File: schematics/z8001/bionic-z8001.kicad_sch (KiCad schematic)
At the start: 9 parts, among them J1 BionicConnector, U1 Z8001, U2 74HCT126, U3 74HCT541, U4 74HCT541

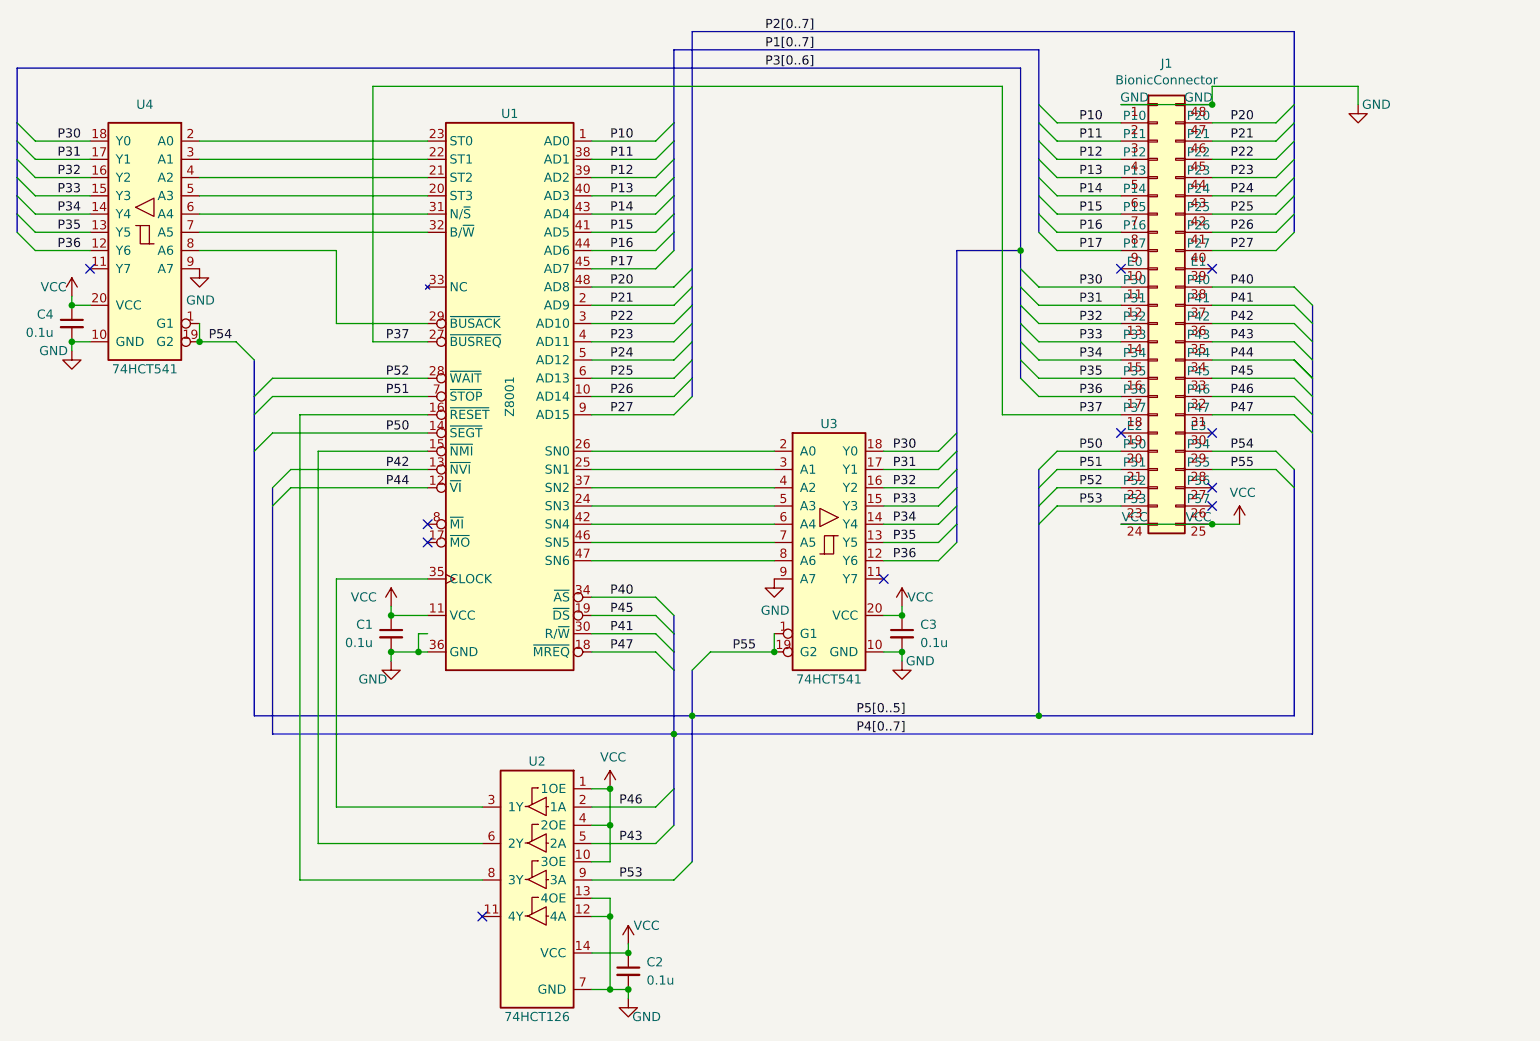
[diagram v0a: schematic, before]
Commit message: [Z8001] Move schematics directory
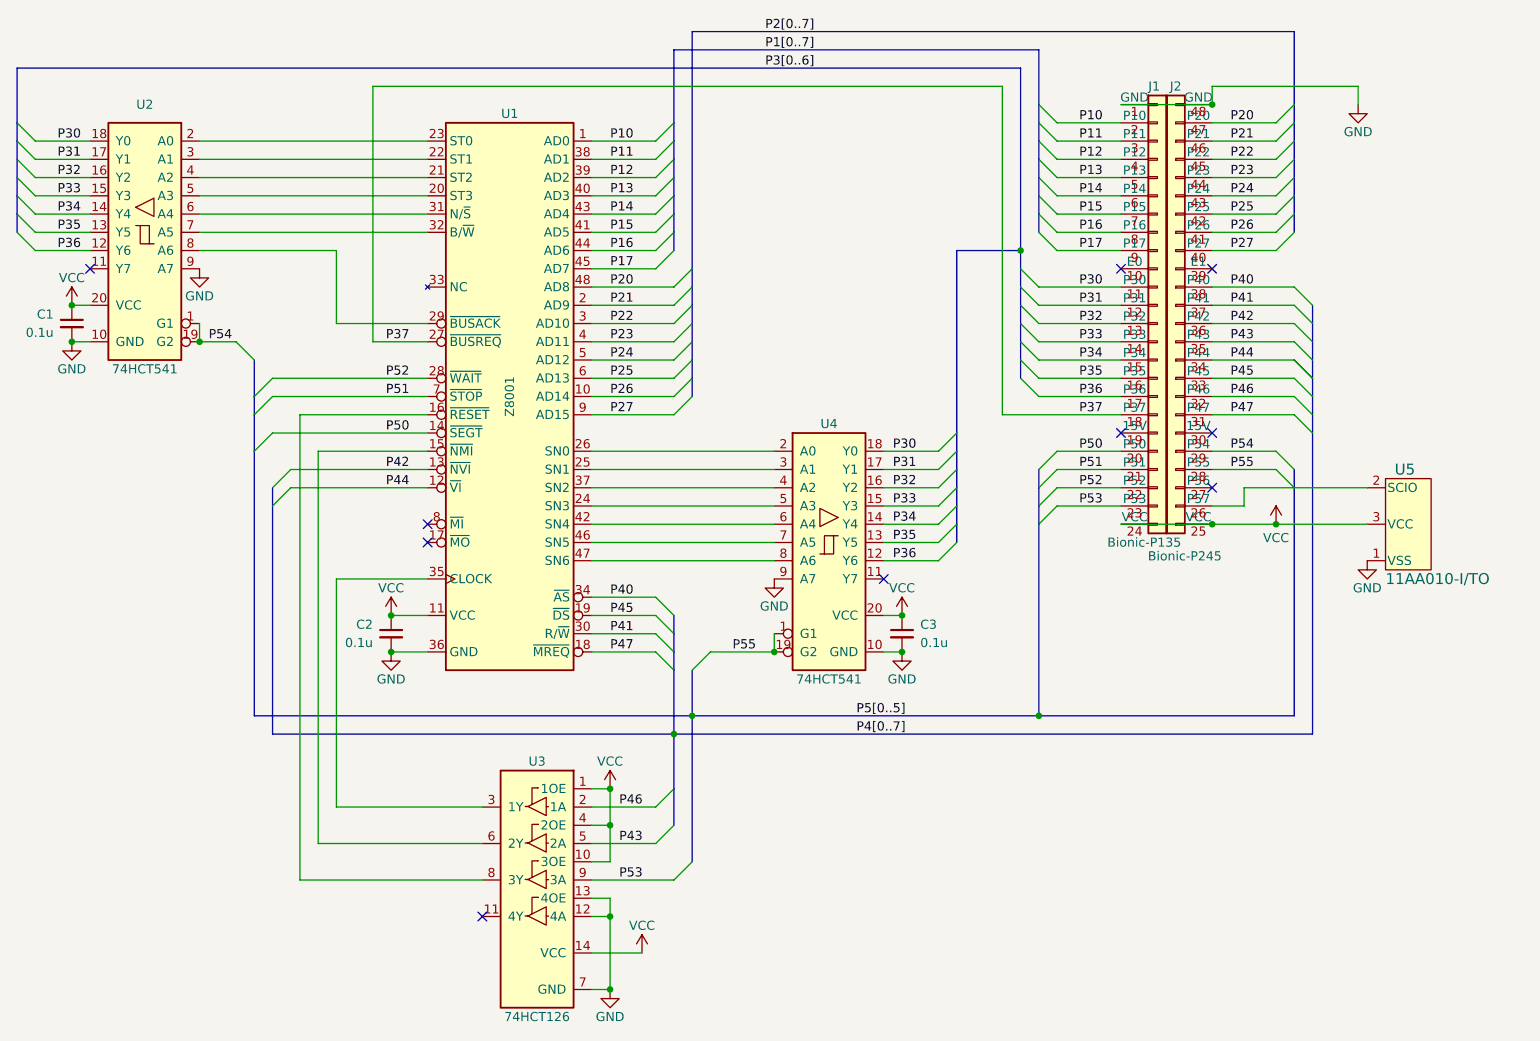
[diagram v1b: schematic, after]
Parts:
- removed C2: 0.1u, Capacitor_THT:C_Disc_D3.4mm_W2.1mm_P2.50mm, symbol Device:C_Small
- removed J1: BionicConnector, 0-LocalLibrary:DIP-48_W7.62mm, symbol 0-LocalLibrary:BionicConnector
- added J1: Bionic-P135, connector:Bionic-P135_Vertical, symbol 0-LocalLibrary:Bionic-P135
- added J2: Bionic-P245, connector:Bionic-P245_Vertical, symbol 0-LocalLibrary:Bionic-P245
- added U5: 11AA010-I/TO, TO-92_MC_MCH, symbol 0-LocalLibrary:11AA010-I_TO
- renumbered C4 to C1, C1 to C2, U4 to U2, U2 to U3, U3 to U4
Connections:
- net GND: now also J1.1 (GND), J2.48 (GND), U5.1 (VSS)
- net P10: now also J1.2 (P10)
- net P11: now also J1.3 (P11)
- net P12: now also J1.4 (P12)
- net P13: now also J1.5 (P13)
- net P14: now also J1.6 (P14)
- net P15: now also J1.7 (P15)
- net P16: now also J1.8 (P16)
- net P17: now also J1.9 (P17)
- net P20: now also J2.47 (P20)
- net P21: now also J2.46 (P21)
- net P22: now also J2.45 (P22)
- net P23: now also J2.44 (P23)
- net P24: now also J2.43 (P24)
- net P25: now also J2.42 (P25)
- net P26: now also J2.41 (P26)
- net P27: now also J2.40 (P27)
- net P30: now also J1.11 (P30)
- net P31: now also J1.12 (P31)
- net P32: now also J1.13 (P32)
- net P33: now also J1.14 (P33)
- net P34: now also J1.15 (P34)
- net P35: now also J1.16 (P35)
- net P36: now also J1.17 (P36)
- net P37: now also J1.18 (P37)
- net P40: now also J2.38 (P40)
- net P41: now also J2.37 (P41)
- net P42: now also J2.36 (P42)
- net P43: now also J2.35 (P43)
- net P44: now also J2.34 (P44)
- net P45: now also J2.33 (P45)
- net P46: now also J2.32 (P46)
- net P47: now also J2.31 (P47)
- net P50: now also J1.20 (P50)
- net P51: now also J1.21 (P51)
- net P52: now also J1.22 (P52)
- net P53: now also J1.23 (P53)
- net P54: now also J2.29 (P54)
- net P55: now also J2.28 (P55)
- net VCC: now also J1.24 (VCC), J2.25 (VCC), U5.3 (VCC)
- new net: J2.26 (P57), U5.2 (SCIO)
- no-connect marks 11 -> 10
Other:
- title: BionicZ8001 Mezzanine -> BionicZ8001
